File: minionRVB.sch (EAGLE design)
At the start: 119 parts, among them IC1 74HCT245DW

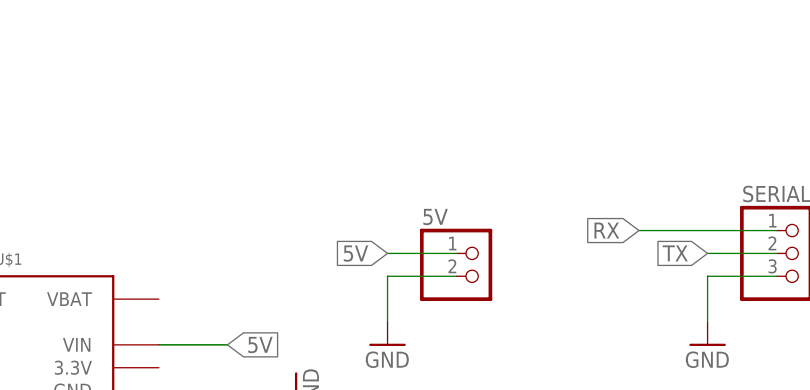
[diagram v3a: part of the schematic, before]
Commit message: Add an optional second alim
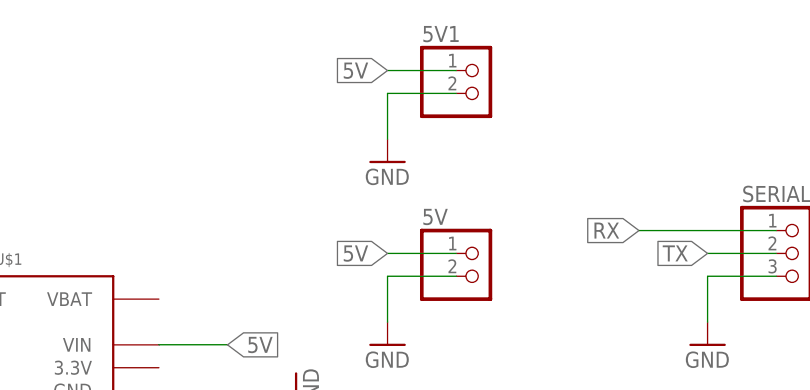
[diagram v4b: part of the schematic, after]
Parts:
- added 5V1: (no value), pinhead:PINHD-1X2
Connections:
- net 5V: now also 5V1.1
- net GND: now also 5V1.2
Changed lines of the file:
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@@
 <part name="GND118" library="SparkFun" deviceset="GND" device=""/>
 <part name="GND119" library="SparkFun" deviceset="GND" device=""/>
+<part name="5V1" library="pinhead" deviceset="PINHD-1X2" device=""/>
+<part name="GND120" library="SparkFun" deviceset="GND" device=""/>
 </parts>
 <sheets>
@@
 <instance part="GND118" gate="1" x="563.88" y="213.36" rot="R180"/>
 <instance part="GND119" gate="1" x="579.12" y="213.36" rot="R180"/>
+<instance part="5V1" gate="G$1" x="386.08" y="236.22"/>
+<instance part="GND120" gate="1" x="375.92" y="228.6"/>
 </instances>
 <busses>
@@
 <wire x1="579.12" y1="203.2" x2="579.12" y2="210.82" width="0.1524" layer="91"/>
 <pinref part="GND119" gate="1" pin="GND"/>
+</segment>
+<segment>
+<pinref part="5V1" gate="G$1" pin="2"/>
+<wire x1="383.54" y1="236.22" x2="375.92" y2="236.22" width="0.1524" layer="91"/>
+<wire x1="375.92" y1="236.22" x2="375.92" y2="231.14" width="0.1524" layer="91"/>
+<pinref part="GND120" gate="1" pin="GND"/>
 </segment>
 </net>
@@
 <label x="530.86" y="228.6" size="1.778" layer="95" rot="R90" xref="yes"/>
 </segment>
-</net>
+<segment>
+<pinref part="5V1" gate="G$1" pin="1"/>
+<wire x1="383.54" y1="238.76" x2="375.92" y2="238.76" width="0.1524" layer="91"/>
+<label x="375.92" y="238.76" size="1.778" layer="95" rot="R180" xref="yes"/>
+</segment>
+</net>

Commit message: Pinswap 5v - signal + DRU OK
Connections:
- net 5V: now also OUTPUT1.2, OUTPUT2.2, OUTPUT3.2, OUTPUT4.2, OUTPUT5.2, OUTPUT6.2, OUTPUT7.2, OUTPUT8.2; no longer OUTPUT1.3, OUTPUT2.3, OUTPUT3.3, OUTPUT4.3, OUTPUT5.3, OUTPUT6.3, OUTPUT7.3, OUTPUT8.3
- net DI: now also INPUT.3; no longer INPUT.2
- net DOUT: now also OUTPUT.3; no longer OUTPUT.2
- net N$42: now also OUTPUT1.3; no longer OUTPUT1.2
- net N$54: now also OUTPUT2.3; no longer OUTPUT2.2
- net N$55: now also OUTPUT3.3; no longer OUTPUT3.2
- net N$56: now also OUTPUT4.3; no longer OUTPUT4.2
- net N$57: now also OUTPUT5.3; no longer OUTPUT5.2
- net N$58: now also OUTPUT6.3; no longer OUTPUT6.2
- net N$59: now also OUTPUT7.3; no longer OUTPUT7.2
- net N$60: now also OUTPUT8.3; no longer OUTPUT8.2
- net VCC: now also INPUT.2, OUTPUT.2; no longer INPUT.3, OUTPUT.3

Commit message: Condo party!!!! \o/
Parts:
- added C53, C54, C55, C56, C57, C58, C59, C60: 0.1uF, SparkFun:CAP0603-CAP
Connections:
- net GND: now also C53.1, C54.1, C55.1, C56.1, C57.1, C58.1, C59.1, C60.1
- net VCC: now also C53.2, C54.2, C55.2, C56.2, C57.2, C58.2, C59.2, C60.2
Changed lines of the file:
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@@
 <part name="5V1" library="pinhead" deviceset="PINHD-1X2" device=""/>
 <part name="GND120" library="SparkFun" deviceset="GND" device=""/>
+<part name="C53" library="SparkFun" deviceset="CAP" device="0603-CAP" value="0.1uF"/>
+<part name="C54" library="SparkFun" deviceset="CAP" device="0603-CAP" value="0.1uF"/>
+<part name="C55" library="SparkFun" deviceset="CAP" device="0603-CAP" value="0.1uF"/>
+<part name="C56" library="SparkFun" deviceset="CAP" device="0603-CAP" value="0.1uF"/>
+<part name="C57" library="SparkFun" deviceset="CAP" device="0603-CAP" value="0.1uF"/>
+<part name="C58" library="SparkFun" deviceset="CAP" device="0603-CAP" value="0.1uF"/>
+<part name="C59" library="SparkFun" deviceset="CAP" device="0603-CAP" value="0.1uF"/>
+<part name="C60" library="SparkFun" deviceset="CAP" device="0603-CAP" value="0.1uF"/>
+<part name="P+107" library="SparkFun" deviceset="VCC" device=""/>
+<part name="GND121" library="SparkFun" deviceset="GND" device=""/>
 </parts>
 <sheets>
@@
 <instance part="5V1" gate="G$1" x="386.08" y="236.22"/>
 <instance part="GND120" gate="1" x="375.92" y="228.6"/>
+<instance part="C53" gate="G$1" x="472.44" y="157.48" rot="R180"/>
+<instance part="C54" gate="G$1" x="482.6" y="157.48" rot="R180"/>
+<instance part="C55" gate="G$1" x="492.76" y="157.48" rot="R180"/>
+<instance part="C56" gate="G$1" x="502.92" y="157.48" rot="R180"/>
+<instance part="C57" gate="G$1" x="513.08" y="157.48" rot="R180"/>
+<instance part="C58" gate="G$1" x="523.24" y="157.48" rot="R180"/>
+<instance part="C59" gate="G$1" x="533.4" y="157.48" rot="R180"/>
+<instance part="C60" gate="G$1" x="543.56" y="157.48" rot="R180"/>
+<instance part="P+107" gate="1" x="508" y="165.1"/>
+<instance part="GND121" gate="1" x="508" y="142.24"/>
 </instances>
 <busses>
@@
 <wire x1="86.36" y1="101.6" x2="91.44" y2="101.6" width="0.1524" layer="91"/>
 </segment>
+<segment>
+<pinref part="C53" gate="G$1" pin="2"/>
+<pinref part="C54" gate="G$1" pin="2"/>
+<wire x1="472.44" y1="160.02" x2="482.6" y2="160.02" width="0.1524" layer="91"/>
+<pinref part="C55" gate="G$1" pin="2"/>
+<wire x1="482.6" y1="160.02" x2="492.76" y2="160.02" width="0.1524" layer="91"/>
+<junction x="482.6" y="160.02"/>
+<pinref part="C56" gate="G$1" pin="2"/>
+<wire x1="492.76" y1="160.02" x2="502.92" y2="160.02" width="0.1524" layer="91"/>
+<junction x="492.76" y="160.02"/>
+<pinref part="C57" gate="G$1" pin="2"/>
+<wire x1="502.92" y1="160.02" x2="508" y2="160.02" width="0.1524" layer="91"/>
+<junction x="502.92" y="160.02"/>
+<pinref part="C58" gate="G$1" pin="2"/>
+<wire x1="508" y1="160.02" x2="513.08" y2="160.02" width="0.1524" layer="91"/>
+<wire x1="513.08" y1="160.02" x2="523.24" y2="160.02" width="0.1524" layer="91"/>
+<junction x="513.08" y="160.02"/>
+<pinref part="C59" gate="G$1" pin="2"/>
+<wire x1="523.24" y1="160.02" x2="533.4" y2="160.02" width="0.1524" layer="91"/>
+<junction x="523.24" y="160.02"/>
+<pinref part="C60" gate="G$1" pin="2"/>
+<wire x1="533.4" y1="160.02" x2="543.56" y2="160.02" width="0.1524" layer="91"/>
+<junction x="533.4" y="160.02"/>
+<wire x1="508" y1="160.02" x2="508" y2="165.1" width="0.1524" layer="91"/>
+<junction x="508" y="160.02"/>
+<pinref part="P+107" gate="1" pin="VCC"/>
+</segment>
 </net>
 <net name="GND" class="0">
@@
 <pinref part="GND120" gate="1" pin="GND"/>
 </segment>
+<segment>
+<pinref part="C60" gate="G$1" pin="1"/>
+<pinref part="C59" gate="G$1" pin="1"/>
+<wire x1="543.56" y1="152.4" x2="533.4" y2="152.4" width="0.1524" layer="91"/>
+<pinref part="C58" gate="G$1" pin="1"/>
+<wire x1="533.4" y1="152.4" x2="523.24" y2="152.4" width="0.1524" layer="91"/>
+<junction x="533.4" y="152.4"/>
+<pinref part="C57" gate="G$1" pin="1"/>
+<wire x1="523.24" y1="152.4" x2="513.08" y2="152.4" width="0.1524" layer="91"/>
+<junction x="523.24" y="152.4"/>
+<pinref part="C56" gate="G$1" pin="1"/>
+<wire x1="502.92" y1="152.4" x2="508" y2="152.4" width="0.1524" layer="91"/>
+<junction x="513.08" y="152.4"/>
+<pinref part="C55" gate="G$1" pin="1"/>
+<wire x1="508" y1="152.4" x2="513.08" y2="152.4" width="0.1524" layer="91"/>
+<wire x1="502.92" y1="152.4" x2="492.76" y2="152.4" width="0.1524" layer="91"/>
+<junction x="502.92" y="152.4"/>
+<pinref part="C54" gate="G$1" pin="1"/>
+<wire x1="492.76" y1="152.4" x2="482.6" y2="152.4" width="0.1524" layer="91"/>
+<junction x="492.76" y="152.4"/>
+<pinref part="C53" gate="G$1" pin="1"/>
+<wire x1="482.6" y1="152.4" x2="472.44" y2="152.4" width="0.1524" layer="91"/>
+<junction x="482.6" y="152.4"/>
+<wire x1="508" y1="152.4" x2="508" y2="144.78" width="0.1524" layer="91"/>
+<junction x="508" y="152.4"/>
+<pinref part="GND121" gate="1" pin="GND"/>
+</segment>
 </net>

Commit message: Update minionRVB
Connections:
- net 5V: now also C53.2, C54.2, C55.2, C56.2, C57.2, C58.2, C59.2, C60.2
- net VCC: no longer C53.2, C54.2, C55.2, C56.2, C57.2, C58.2, C59.2, C60.2
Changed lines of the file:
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@@
 <part name="C59" library="SparkFun" deviceset="CAP" device="0603-CAP" value="0.1uF"/>
 <part name="C60" library="SparkFun" deviceset="CAP" device="0603-CAP" value="0.1uF"/>
-<part name="P+107" library="SparkFun" deviceset="VCC" device=""/>
 <part name="GND121" library="SparkFun" deviceset="GND" device=""/>
 </parts>
@@
 <instance part="C59" gate="G$1" x="533.4" y="157.48" rot="R180"/>
 <instance part="C60" gate="G$1" x="543.56" y="157.48" rot="R180"/>
-<instance part="P+107" gate="1" x="508" y="165.1"/>
 <instance part="GND121" gate="1" x="508" y="142.24"/>
 </instances>
@@
 <pinref part="P+4" gate="1" pin="VCC"/>
 <wire x1="86.36" y1="101.6" x2="91.44" y2="101.6" width="0.1524" layer="91"/>
-</segment>
-<segment>
-<pinref part="C53" gate="G$1" pin="2"/>
-<pinref part="C54" gate="G$1" pin="2"/>
-<wire x1="472.44" y1="160.02" x2="482.6" y2="160.02" width="0.1524" layer="91"/>
-<pinref part="C55" gate="G$1" pin="2"/>
-<wire x1="482.6" y1="160.02" x2="492.76" y2="160.02" width="0.1524" layer="91"/>
-<junction x="482.6" y="160.02"/>
-<pinref part="C56" gate="G$1" pin="2"/>
-<wire x1="492.76" y1="160.02" x2="502.92" y2="160.02" width="0.1524" layer="91"/>
-<junction x="492.76" y="160.02"/>
-<pinref part="C57" gate="G$1" pin="2"/>
-<wire x1="502.92" y1="160.02" x2="508" y2="160.02" width="0.1524" layer="91"/>
-<junction x="502.92" y="160.02"/>
-<pinref part="C58" gate="G$1" pin="2"/>
-<wire x1="508" y1="160.02" x2="513.08" y2="160.02" width="0.1524" layer="91"/>
-<wire x1="513.08" y1="160.02" x2="523.24" y2="160.02" width="0.1524" layer="91"/>
-<junction x="513.08" y="160.02"/>
-<pinref part="C59" gate="G$1" pin="2"/>
-<wire x1="523.24" y1="160.02" x2="533.4" y2="160.02" width="0.1524" layer="91"/>
-<junction x="523.24" y="160.02"/>
-<pinref part="C60" gate="G$1" pin="2"/>
-<wire x1="533.4" y1="160.02" x2="543.56" y2="160.02" width="0.1524" layer="91"/>
-<junction x="533.4" y="160.02"/>
-<wire x1="508" y1="160.02" x2="508" y2="165.1" width="0.1524" layer="91"/>
-<junction x="508" y="160.02"/>
-<pinref part="P+107" gate="1" pin="VCC"/>
 </segment>
 </net>
@@
 <label x="375.92" y="238.76" size="1.778" layer="95" rot="R180" xref="yes"/>
 </segment>
-</net>
+<segment>
+<pinref part="C53" gate="G$1" pin="2"/>
+<pinref part="C54" gate="G$1" pin="2"/>
+<wire x1="472.44" y1="160.02" x2="482.6" y2="160.02" width="0.1524" layer="91"/>
+<pinref part="C55" gate="G$1" pin="2"/>
+<wire x1="482.6" y1="160.02" x2="492.76" y2="160.02" width="0.1524" layer="91"/>
+<junction x="482.6" y="160.02"/>
+<pinref part="C56" gate="G$1" pin="2"/>
+<wire x1="492.76" y1="160.02" x2="502.92" y2="160.02" width="0.1524" layer="91"/>
+<junction x="492.76" y="160.02"/>
+<pinref part="C57" gate="G$1" pin="2"/>
+<wire x1="502.92" y1="160.02" x2="508" y2="160.02" width="0.1524" layer="91"/>
+<junction x="502.92" y="160.02"/>
+<pinref part="C58" gate="G$1" pin="2"/>
+<wire x1="508" y1="160.02" x2="513.08" y2="160.02" width="0.1524" layer="91"/>
+<wire x1="513.08" y1="160.02" x2="523.24" y2="160.02" width="0.1524" layer="91"/>
+<junction x="513.08" y="160.02"/>
+<pinref part="C59" gate="G$1" pin="2"/>
+<wire x1="523.24" y1="160.02" x2="533.4" y2="160.02" width="0.1524" layer="91"/>
+<junction x="523.24" y="160.02"/>
+<pinref part="C60" gate="G$1" pin="2"/>
+<wire x1="533.4" y1="160.02" x2="543.56" y2="160.02" width="0.1524" layer="91"/>
+<junction x="533.4" y="160.02"/>
+<wire x1="508" y1="160.02" x2="508" y2="165.1" width="0.1524" layer="91"/>
+<junction x="508" y="160.02"/>
+<label x="508" y="165.1" size="1.778" layer="95" rot="R90" xref="yes"/>
+</segment>
+</net>
